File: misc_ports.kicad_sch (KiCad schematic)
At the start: 34 parts, among them J10 Molex 46765-2301, J3 Wuerth_7499010121A, J7 QMTECH JTAG, J8 RTC, J9 1140084168 microSD Card Slot, P1 Full-side CD Card Slot, U12 DP83826, U13 74LVC374, U14 PTN3363BSMP

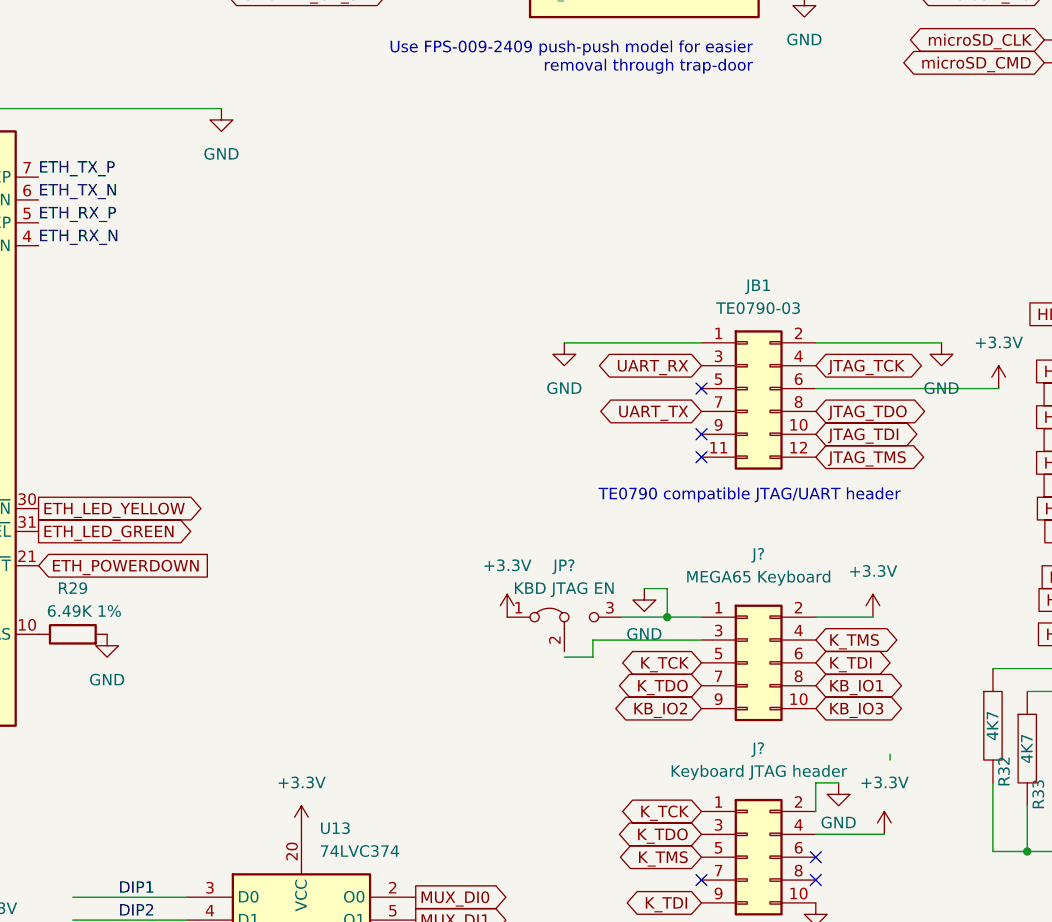
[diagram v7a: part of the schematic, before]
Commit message: add USB blaster JTAG and bare UART headers #11
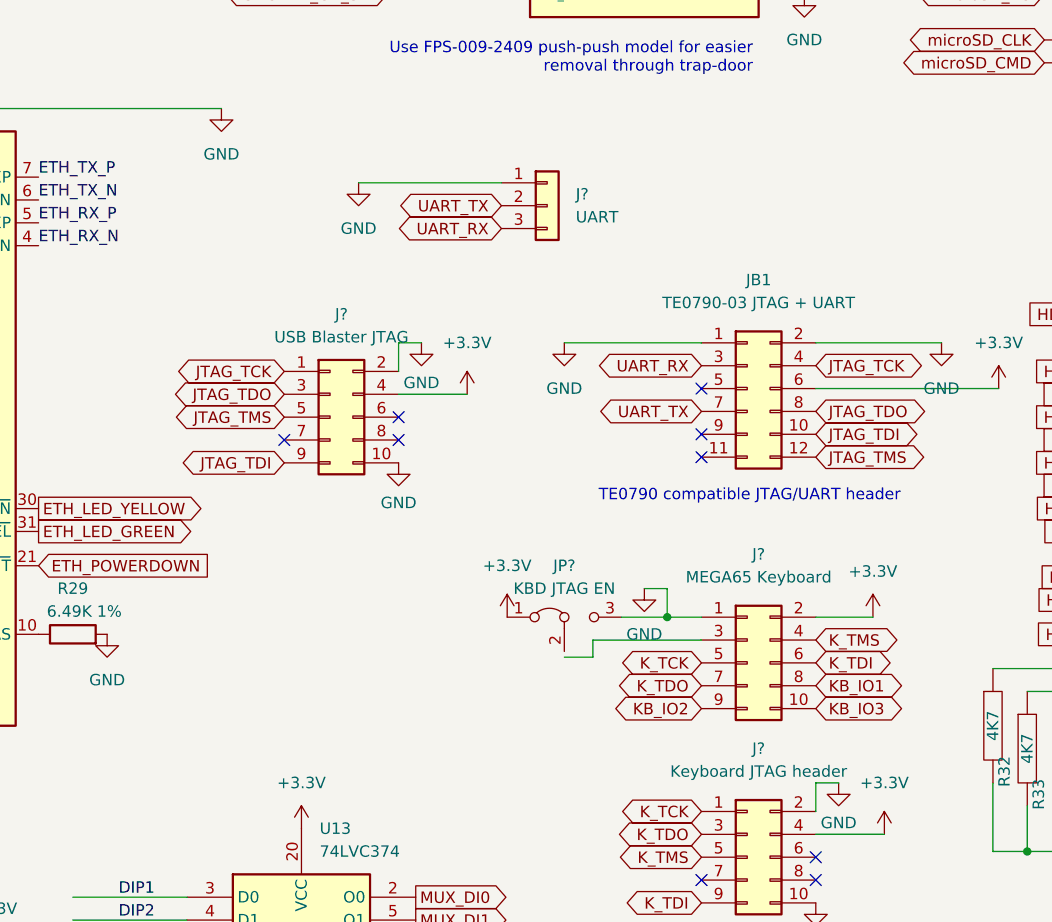
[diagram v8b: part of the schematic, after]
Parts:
- added J?: UART, Connector_PinHeader_2.54mm:PinHeader_1x03_P2.54mm_Vertical, symbol Connector_Generic:Conn_01x03
- added J?: USB Blaster JTAG, Connector_PinHeader_2.54mm:PinHeader_2x05_P2.54mm_Vertical, symbol Connector_Generic:Conn_02x05_Odd_Even
- JB1: value TE0790-03 -> TE0790-03 JTAG + UART
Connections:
- net +3V3: now also J?.4 (Pin_4)
- net GND: now also J?.1 (Pin_1), J?.10 (Pin_10), J?.2 (Pin_2)
- net JTAG_TCK: now also J?.1 (Pin_1)
- net JTAG_TDI: now also J?.9 (Pin_9)
- net JTAG_TDO: now also J?.3 (Pin_3)
- net JTAG_TMS: now also J?.5 (Pin_5)
- net UART_RX: now also J?.3 (Pin_3)
- net UART_TX: now also J?.2 (Pin_2)
- no-connect marks 14 -> 17
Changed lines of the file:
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@@
   (no_connect (at 31.75 135.89))
   (no_connect (at 31.75 80.01))
+  (no_connect (at 99.695 106.68))
   (no_connect (at 146.05 108.585))
   (no_connect (at 146.05 106.045))
@@
   (no_connect (at 148.59 176.53))
   (no_connect (at 31.75 100.33))
+  (no_connect (at 112.395 104.14))
   (no_connect (at 31.75 97.79))
   (no_connect (at 146.05 155.575))
   (no_connect (at 255.905 15.875))
+  (no_connect (at 112.395 106.68))
   (no_connect (at 259.08 134.62))
   (no_connect (at 31.75 82.55))
@@
     (stroke (width 0) (type default) (color 0 0 0 0))
   )
+  (wire (pts (xy 112.395 99.06) (xy 112.395 95.885))
+    (stroke (width 0) (type default) (color 0 0 0 0))
+  )
   (wire (pts (xy 224.155 92.71) (xy 224.155 95.25))
     (stroke (width 0) (type default) (color 0 0 0 0))
@@
     (stroke (width 0) (type default) (color 0 0 0 0))
   )
+  (wire (pts (xy 112.395 95.885) (xy 114.935 95.885))
+    (stroke (width 0) (type default) (color 0 0 0 0))
+  )
   (wire (pts (xy 41.91 16.51) (xy 41.91 21.59))
     (stroke (width 0) (type default) (color 0 0 0 0))
@@
     (stroke (width 0) (type default) (color 0 0 0 0))
   )
+  (wire (pts (xy 112.395 101.6) (xy 120.015 101.6))
+    (stroke (width 0) (type default) (color 0 0 0 0))
+  )
   (wire (pts (xy 182.245 147.32) (xy 182.245 152.4))
     (stroke (width 0) (type default) (color 0 0 0 0))
@@
     (stroke (width 0) (type default) (color 0 0 0 0))
   )
+  (wire (pts (xy 107.95 78.105) (xy 123.825 78.105))
+    (stroke (width 0) (type default) (color 0 0 0 0))
+  )
   (wire (pts (xy 224.155 111.76) (xy 259.08 111.76))
     (stroke (width 0) (type default) (color 0 0 0 0))
@@
   )
   (wire (pts (xy 236.22 132.08) (xy 257.175 132.08))
-    (stroke (width 0) (type default) (color 0 0 0 0))
-  )
-  (wire (pts (xy 167.005 142.24) (xy 167.005 141.605))
     (stroke (width 0) (type default) (color 0 0 0 0))
   )
@@
     )
   )
+  (global_label "JTAG_TDI" (shape bidirectional) (at 99.695 109.22 180) (fields_autoplaced)
+    (effects (font (size 1.27 1.27)) (justify right))
+    (property "Intersheet References" "${INTERSHEET_REFS}" (id 0) (at 89.1781 109.1406 0)
+      (effects (font (size 1.27 1.27)) (justify right) hide)
+    )
+  )
   (global_label "microSD_CLK" (shape bidirectional) (at 184.15 62.23 180) (fields_autoplaced)
     (effects (font (size 1.27 1.27)) (justify right))
@@
     )
   )
+  (global_label "JTAG_TDO" (shape bidirectional) (at 99.695 101.6 180) (fields_autoplaced)
+    (effects (font (size 1.27 1.27)) (justify right))
+    (property "Intersheet References" "${INTERSHEET_REFS}" (id 0) (at 88.4524 101.5206 0)
+      (effects (font (size 1.27 1.27)) (justify right) hide)
+    )
+  )
   (global_label "ETH_RX_CLK" (shape output) (at 31.75 105.41 180) (fields_autoplaced)
     (effects (font (size 1.27 1.27)) (justify right))
@@
     (effects (font (size 1.27 1.27)) (justify right))
     (property "Intersheet References" "${INTERSHEET_REFS}" (id 0) (at 182.8557 109.1406 0)
+      (effects (font (size 1.27 1.27)) (justify right) hide)
+    )
+  )
+  (global_label "JTAG_TMS" (shape bidirectional) (at 99.695 104.14 180) (fields_autoplaced)
+    (effects (font (size 1.27 1.27)) (justify right))
+    (property "Intersheet References" "${INTERSHEET_REFS}" (id 0) (at 88.3919 104.0606 0)
       (effects (font (size 1.27 1.27)) (justify right) hide)
     )
@@
     )
   )
+  (global_label "JTAG_TCK" (shape bidirectional) (at 99.695 99.06 180) (fields_autoplaced)
+    (effects (font (size 1.27 1.27)) (justify right))
+    (property "Intersheet References" "${INTERSHEET_REFS}" (id 0) (at 88.5129 98.9806 0)
+      (effects (font (size 1.27 1.27)) (justify right) hide)
+    )
+  )
   (global_label "HDMI_D1+" (shape input) (at 194.945 104.14 180) (fields_autoplaced)
     (effects (font (size 1.27 1.27)) (justify right))
     (property "Intersheet References" "${INTERSHEET_REFS}" (id 0) (at 182.8557 104.0606 0)
+      (effects (font (size 1.27 1.27)) (justify right) hide)
+    )
+  )
+  (global_label "UART_RX" (shape bidirectional) (at 123.825 83.185 180) (fields_autoplaced)
+    (effects (font (size 1.27 1.27)) (justify right))
+    (property "Intersheet References" "${INTERSHEET_REFS}" (id 0) (at 113.3081 83.1056 0)
       (effects (font (size 1.27 1.27)) (justify right) hide)
     )
@@
     )
   )
+  (global_label "UART_TX" (shape bidirectional) (at 123.825 80.645 180) (fields_autoplaced)
+    (effects (font (size 1.27 1.27)) (justify right))
+    (property "Intersheet References" "${INTERSHEET_REFS}" (id 0) (at 113.6105 80.5656 0)
+      (effects (font (size 1.27 1.27)) (justify right) hide)
+    )
+  )
   (global_label "ETH_LED_GREEN" (shape input) (at 44.45 21.59 0) (fields_autoplaced)
     (effects (font (size 1.27 1.27)) (justify left))
@@
       (effects (font (size 1.27 1.27)) (justify left) hide)
     )
+  )
+  (symbol (lib_id "Connector_Generic:Conn_01x03") (at 128.905 80.645 0) (unit 1)
+    (in_bom yes) (on_board yes) (fields_autoplaced)
+    (property "Reference" "J?" (id 0) (at 132.08 79.3749 0)
+      (effects (font (size 1.27 1.27)) (justify left))
+    )
+    (property "Value" "UART" (id 1) (at 132.08 81.9149 0)
+      (effects (font (size 1.27 1.27)) (justify left))
+    )
+    (property "Footprint" "Connector_PinHeader_2.54mm:PinHeader_1x03_P2.54mm_Vertical" (id 2) (at 128.905 80.645 0)
+      (effects (font (size 1.27 1.27)) hide)
+    )
+    (property "Datasheet" "~" (id 3) (at 128.905 80.645 0)
+      (effects (font (size 1.27 1.27)) hide)
+    )
+    (pin "1")
+    (pin "2")
+    (pin "3")
   )
   (symbol (lib_id "Device:R") (at 30.48 16.51 90) (unit 1)
@@
     (pin "1")
     (pin "2")
+  )
+  (symbol (lib_id "power:GND") (at 112.395 109.22 0) (unit 1)
+    (in_bom yes) (on_board yes) (fields_autoplaced)
+    (property "Reference" "#PWR?" (id 0) (at 112.395 115.57 0)
+      (effects (font (size 1.27 1.27)) hide)
+    )
+    (property "Value" "GND" (id 1) (at 112.395 113.665 0))
+    (property "Footprint" "" (id 2) (at 112.395 109.22 0)
+      (effects (font (size 1.27 1.27)) hide)
+    )
+    (property "Datasheet" "" (id 3) (at 112.395 109.22 0)
+      (effects (font (size 1.27 1.27)) hide)
+    )
+    (pin "1")
   )
   (symbol (lib_id "Device:C") (at 27.94 63.5 0) (unit 1)
@@
   (symbol (lib_id "Connector_Generic:Conn_02x06_Odd_Even") (at 151.13 100.965 0) (unit 1)
     (in_bom yes) (on_board yes) (fields_autoplaced)
-    (property "Reference" "JB1" (id 0) (at 152.4 89.535 0))
-    (property "Value" "TE0790-03" (id 1) (at 152.4 92.075 0))
+    (property "Reference" "JB1" (id 0) (at 152.4 88.9 0))
+    (property "Value" "TE0790-03 JTAG + UART" (id 1) (at 152.4 91.44 0))
     (property "Footprint" "Connector_PinHeader_2.54mm:PinHeader_2x06_P2.54mm_Vertical" (id 2) (at 151.13 100.965 0)
       (effects (font (size 1.27 1.27)) hide)
@@
     (pin "2")
   )
+  (symbol (lib_id "Connector_Generic:Conn_02x05_Odd_Even") (at 104.775 104.14 0) (unit 1)
+    (in_bom yes) (on_board yes) (fields_autoplaced)
+    (property "Reference" "J?" (id 0) (at 106.045 92.71 0))
+    (property "Value" "USB Blaster JTAG" (id 1) (at 106.045 95.25 0))
+    (property "Footprint" "Connector_PinHeader_2.54mm:PinHeader_2x05_P2.54mm_Vertical" (id 2) (at 104.775 104.14 0)
+      (effects (font (size 1.27 1.27)) hide)
+    )
+    (property "Datasheet" "~" (id 3) (at 104.775 104.14 0)
+      (effects (font (size 1.27 1.27)) hide)
+    )
+    (pin "1")
+    (pin "10")
+    (pin "2")
+    (pin "3")
+    (pin "4")
+    (pin "5")
+    (pin "6")
+    (pin "7")
+    (pin "8")
+    (pin "9")
+  )
   (symbol (lib_id "power:GND") (at 161.29 144.78 0) (unit 1)
     (in_bom yes) (on_board yes) (fields_autoplaced)
@@
     )
     (property "Datasheet" "" (id 3) (at 161.29 144.78 0)
+      (effects (font (size 1.27 1.27)) hide)
+    )
+    (pin "1")
+  )
+  (symbol (lib_id "power:GND") (at 114.935 95.885 0) (unit 1)
+    (in_bom yes) (on_board yes) (fields_autoplaced)
+    (property "Reference" "#PWR?" (id 0) (at 114.935 102.235 0)
+      (effects (font (size 1.27 1.27)) hide)
+    )
+    (property "Value" "GND" (id 1) (at 114.935 100.33 0))
+    (property "Footprint" "" (id 2) (at 114.935 95.885 0)
+      (effects (font (size 1.27 1.27)) hide)
+    )
+    (property "Datasheet" "" (id 3) (at 114.935 95.885 0)
       (effects (font (size 1.27 1.27)) hide)
     )
@@
     )
     (property "Datasheet" "" (id 3) (at 101.6 190.5 0)
+      (effects (font (size 1.27 1.27)) hide)
+    )
+    (pin "1")
+  )
+  (symbol (lib_id "power:GND") (at 107.95 78.105 0) (unit 1)
+    (in_bom yes) (on_board yes) (fields_autoplaced)
+    (property "Reference" "#PWR?" (id 0) (at 107.95 84.455 0)
+      (effects (font (size 1.27 1.27)) hide)
+    )
+    (property "Value" "GND" (id 1) (at 107.95 83.185 0))
+    (property "Footprint" "" (id 2) (at 107.95 78.105 0)
+      (effects (font (size 1.27 1.27)) hide)
+    )
+    (property "Datasheet" "" (id 3) (at 107.95 78.105 0)
       (effects (font (size 1.27 1.27)) hide)
     )
@@
     (pin "A8")
   )
+  (symbol (lib_id "power:+3.3V") (at 120.015 101.6 0) (unit 1)
+    (in_bom yes) (on_board yes) (fields_autoplaced)
+    (property "Reference" "#PWR?" (id 0) (at 120.015 105.41 0)
+      (effects (font (size 1.27 1.27)) hide)
+    )
+    (property "Value" "+3.3V" (id 1) (at 120.015 95.885 0))
+    (property "Footprint" "" (id 2) (at 120.015 101.6 0)
+      (effects (font (size 1.27 1.27)) hide)
+    )
+    (property "Datasheet" "" (id 3) (at 120.015 101.6 0)
+      (effects (font (size 1.27 1.27)) hide)
+    )
+    (pin "1")
+  )
   (symbol (lib_id "power:GND") (at 158.75 158.115 0) (unit 1)
